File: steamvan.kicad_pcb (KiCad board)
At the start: 2 copper layers, 0 parts

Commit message: Add: new minivan layouts, and start switching to MX/Alps hybrid footprints
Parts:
- added C1: 30p, Capacitor_SMD:C_0603_1608Metric, F.Cu at (-222.7, 200.6)
- added C10: 1u, Capacitor_SMD:C_0603_1608Metric, F.Cu at (-221.6, 197.2)
- added C11: 1u, Capacitor_SMD:C_0603_1608Metric, F.Cu at (-226.3, 203.6)
- added C2: 30p, Capacitor_SMD:C_0603_1608Metric, F.Cu at (-218.5, 195.7)
- added C3: 100n, Capacitor_SMD:C_0603_1608Metric, F.Cu at (-221.6, 194.2)
- added C4: 100n, Capacitor_SMD:C_0603_1608Metric, F.Cu at (-229.3, 202.9)
- added C5: 4.7u, Capacitor_SMD:C_0603_1608Metric, F.Cu at (-225.5, 202.1)
- added C6: 1u, Capacitor_SMD:C_0603_1608Metric, F.Cu at (-229.3, 204.4)
- added C7: 10n, Capacitor_SMD:C_0603_1608Metric, F.Cu at (-218.5, 194.2)
- added C8: 100n, Capacitor_SMD:C_0603_1608Metric, F.Cu at (-221.6, 195.7)
- added C9: 100n, Capacitor_SMD:C_0603_1608Metric, F.Cu at (-222.7, 199.1)
- added D1: D, Diode_SMD:D_SOD-123, F.Cu at (-176.2, 181.4)
- added D10: D, Diode_SMD:D_SOD-123, F.Cu at (-203.8, 181.4)
- added D11: D, Diode_SMD:D_SOD-123, F.Cu at (-207.2, 181.4)
- added D12: D, Diode_SMD:D_SOD-123, F.Cu at (-210.7, 181.4)
- added D13: D, Diode_SMD:D_SOD-123, F.Cu at (-214.1, 181.4)
- added D14: D, Diode_SMD:D_SOD-123, F.Cu at (-217.6, 181.4)
- added D15: D, Diode_SMD:D_SOD-123, F.Cu at (-221.0, 181.4)
- added D16: D, Diode_SMD:D_SOD-123, F.Cu at (-224.5, 181.4)
- added D17: D, Diode_SMD:D_SOD-123, F.Cu at (-227.9, 181.4)
- added D18: D, Diode_SMD:D_SOD-123, F.Cu at (-231.4, 181.4)
- added D19: D, Diode_SMD:D_SOD-123, F.Cu at (-234.8, 181.4)
- added D2: D, Diode_SMD:D_SOD-123, F.Cu at (-179.6, 181.4)
- added D20: D, Diode_SMD:D_SOD-123, F.Cu at (-169.3, 181.4)
- added D21: D, Diode_SMD:D_SOD-123, F.Cu at (-238.3, 181.4)
- added D22: D, Diode_SMD:D_SOD-123, F.Cu at (-245.2, 181.4)
- added D23: D, Diode_SMD:D_SOD-123, F.Cu at (-183.1, 181.4)
- added D24: D, Diode_SMD:D_SOD-123, F.Cu at (-135.1, 221.1)
- added D25: D, Diode_SMD:D_SOD-123, F.Cu at (-96.7, 182.7)
- added D26: D, Diode_SMD:D_SOD-123, F.Cu at (-130.4, 221.1)
- added D27: D, Diode_SMD:D_SOD-123, F.Cu at (-92.0, 182.7)
- added D28: D, Diode_SMD:D_SOD-123, F.Cu at (-96.7, 185.0)
- added D29: D, Diode_SMD:D_SOD-123, F.Cu at (-96.7, 187.4)
- added D3: D, Diode_SMD:D_SOD-123, F.Cu at (-241.7, 181.4)
- added D30: D, Diode_SMD:D_SOD-123, F.Cu at (-96.7, 189.7)
- added D31: D, Diode_SMD:D_SOD-123, F.Cu at (-92.0, 185.0)
- added D32: D, Diode_SMD:D_SOD-123, F.Cu at (-96.7, 192.1)
- added D33: D, Diode_SMD:D_SOD-123, F.Cu at (-87.2, 182.7)
- added D34: D, Diode_SMD:D_SOD-123, F.Cu at (-92.0, 187.4)
- added D35: D, Diode_SMD:D_SOD-123, F.Cu at (-125.6, 221.1)
- added D36: D, Diode_SMD:D_SOD-123, F.Cu at (-92.0, 189.7)
- added D37: D, Diode_SMD:D_SOD-123, F.Cu at (-96.7, 194.4)
- added D38: D, Diode_SMD:D_SOD-123, F.Cu at (-87.2, 185.0)
- added D39: D, Diode_SMD:D_SOD-123, F.Cu at (-92.0, 192.1)
- added D4: D, Diode_SMD:D_SOD-123, F.Cu at (-172.7, 181.4)
- added D40: D, Diode_SMD:D_SOD-123, F.Cu at (-96.7, 196.8)
- added D41: D, Diode_SMD:D_SOD-123, F.Cu at (-82.5, 182.7)
- added D42: D, Diode_SMD:D_SOD-123, F.Cu at (-87.2, 187.4)
- added D43: D, Diode_SMD:D_SOD-123, F.Cu at (-120.9, 221.1)
- added D44: D, Diode_SMD:D_SOD-123, F.Cu at (-87.2, 189.7)
- added D45: D, Diode_SMD:D_SOD-123, F.Cu at (-96.7, 199.1)
- added D46: D, Diode_SMD:D_SOD-123, F.Cu at (-92.0, 194.4)
- added D5: D, Diode_SMD:D_SOD-123, F.Cu at (-186.5, 181.4)
- added D6: D, Diode_SMD:D_SOD-123, F.Cu at (-190.0, 181.4)
- added D7: D, Diode_SMD:D_SOD-123, F.Cu at (-193.4, 181.4)
- added D8: D, Diode_SMD:D_SOD-123, F.Cu at (-196.9, 181.4)
- added D9: D, Diode_SMD:D_SOD-123, F.Cu at (-200.3, 181.4)
- added F1: 500mA, Resistor_SMD:R_0805_2012Metric, F.Cu at (-245.2, 204.3)
- added J1: Conn_01x05_Male, Connector_PinHeader_2.54mm:PinHeader_1x05_P2.54mm_Vertical, F.Cu at (-245.1, 191.3)
- added K_,1: MX-1U, MX_Alps_Hybrid:MX-1U, F.Cu at (247.7, 103.2)
- added K_.1: MX-1U, MX_Alps_Hybrid:MX-1U, F.Cu at (266.7, 103.2)
- added K_/1: MX-1U, MX_Alps_Hybrid:MX-1U, F.Cu at (285.8, 103.2)
- added K_;1: MX-1U, MX_Alps_Hybrid:MX-1U, F.Cu at (276.2, 84.1)
- added K_A1: MX-1U, MX_Alps_Hybrid:MX-1U, F.Cu at (104.8, 84.1)
- added K_B1: MX-1U, MX_Alps_Hybrid:MX-1U, F.Cu at (190.5, 103.2)
- added K_BACK1: MX-1.75U, MX_Alps_Hybrid:MX-1.75U, F.Cu at (297.7, 65.1)
- added K_C1: MX-1U, MX_Alps_Hybrid:MX-1U, F.Cu at (152.4, 103.2)
- added K_D1: MX-1U, MX_Alps_Hybrid:MX-1U, F.Cu at (142.9, 84.1)
- added K_DOWN1: MX-1U, MX_Alps_Hybrid:MXOnly-1U, F.Cu at (285.8, 122.2)
- added K_E1: MX-1U, MX_Alps_Hybrid:MX-1U, F.Cu at (138.1, 65.1)
- added K_ENTER1: MX-2.25U, MX_Alps_Hybrid:MXOnly-2.25U-ReversedStabilizers, F.Cu at (169.1, 122.2)
- added K_F1: MX-1U, MX_Alps_Hybrid:MX-1U, F.Cu at (161.9, 84.1)
- added K_FN1: MX-1.25U, MX_Alps_Hybrid:MX-1.25U, F.Cu at (83.3, 84.1)
- added K_FN2: MX-1.5U, MX_Alps_Hybrid:MX-1.5U, F.Cu at (300.0, 84.1)
- added K_FN3: MX-1U, MX_Alps_Hybrid:MX-1U, F.Cu at (304.8, 103.2)
- added K_FN4: MX-1.5U, MX_Alps_Hybrid:MXOnly-1.5U, F.Cu at (109.5, 122.2)
- added K_FN4_2: MX-1U, MX_Alps_Hybrid:MX-1U, F.Cu at (-108.7, 210.3)
- added K_G1: MX-1U, MX_Alps_Hybrid:MX-1U, F.Cu at (181.0, 84.1)
- added K_H1: MX-1U, MX_Alps_Hybrid:MX-1U, F.Cu at (200.0, 84.1)
- added K_I1: MX-1U, MX_Alps_Hybrid:MX-1U, F.Cu at (233.4, 65.1)
- added K_J1: MX-1U, MX_Alps_Hybrid:MX-1U, F.Cu at (219.1, 84.1)
- added K_K1: MX-1U, MX_Alps_Hybrid:MX-1U, F.Cu at (238.1, 84.1)
- added K_L1: MX-1U, MX_Alps_Hybrid:MX-1U, F.Cu at (257.2, 84.1)
- added K_LALT1: MX-1U, MX_Alps_Hybrid:MX-1U, F.Cu at (-108.7, 191.1)
- added K_LCTL1: MX-1.25U, MX_Alps_Hybrid:MXOnly-1.25U, F.Cu at (83.3, 122.2)
- added K_LCTL2: MX-1U, MX_Alps_Hybrid:MX-1U, F.Cu at (-127.9, 210.3)
- added K_LOCK1: MX-1.75U, MX_Alps_Hybrid:MXOnly-1.75U, F.Cu at (297.7, 122.2)
- added K_LSHIFT1: MX-1.75U, MX_Alps_Hybrid:MX-1.75U, F.Cu at (88.1, 103.2)
- added K_M1: MX-1U, MX_Alps_Hybrid:MX-1U, F.Cu at (228.6, 103.2)
- added K_N1: MX-1U, MX_Alps_Hybrid:MX-1U, F.Cu at (209.6, 103.2)
- added K_O1: MX-1U, MX_Alps_Hybrid:MX-1U, F.Cu at (252.4, 65.1)
- added K_P1: MX-1U, MX_Alps_Hybrid:MX-1U, F.Cu at (271.5, 65.1)
- added K_Q1: MX-1U, MX_Alps_Hybrid:MX-1U, F.Cu at (100.0, 65.1)
- added K_R1: MX-1U, MX_Alps_Hybrid:MX-1U, F.Cu at (157.2, 65.1)
- added K_RALT1: MX-1.25U, MX_Alps_Hybrid:MXOnly-1.25U, F.Cu at (240.5, 122.2)
- added K_RALT2: MX-1.5U, MX_Alps_Hybrid:MXOnly-1.5U-FLIPPED, F.Cu at (242.9, 122.2)
- added K_RIGHT1: MX-1U, MX_Alps_Hybrid:MXOnly-1U, F.Cu at (304.8, 122.2)
- added K_RSHIFT1: MX-1.5U, MX_Alps_Hybrid:MXOnly-1.5U, F.Cu at (266.7, 122.2)
- added K_S1: MX-1U, MX_Alps_Hybrid:MX-1U, F.Cu at (123.8, 84.1)
- added K_SPACE1: MX-2U, MX_Alps_Hybrid:MXOnly-2U-ReversedStabilizers, F.Cu at (209.6, 122.2)
- added K_SUPER1: MX-1.25U, MX_Alps_Hybrid:MXOnly-1.25U, F.Cu at (135.7, 122.2)
- added K_SUPER2: MX-1U, MX_Alps_Hybrid:MX-1U, F.Cu at (-127.9, 191.1)
- added K_T1: MX-1U, MX_Alps_Hybrid:MX-1U, F.Cu at (176.2, 65.1)
- added K_TAB1: MX-1U, MX_Alps_Hybrid:MX-1U, F.Cu at (81.0, 65.1)
- added K_U1: MX-1U, MX_Alps_Hybrid:MX-1U, F.Cu at (214.3, 65.1)
- added K_V1: MX-1U, MX_Alps_Hybrid:MX-1U, F.Cu at (171.4, 103.2)
- added K_W1: MX-1U, MX_Alps_Hybrid:MX-1U, F.Cu at (119.1, 65.1)
- added K_X1: MX-1U, MX_Alps_Hybrid:MX-1U, F.Cu at (133.3, 103.2)
- added K_Y1: MX-1U, MX_Alps_Hybrid:MX-1U, F.Cu at (195.3, 65.1)
- added K_Z1: MX-1U, MX_Alps_Hybrid:MX-1U, F.Cu at (114.3, 103.2)
- added Q1: FMMT493TA, digikey-footprints:SOT-23-3, F.Cu at (-221.2, 191.5)
- added R1: 560, Resistor_SMD:R_0603_1608Metric, F.Cu at (-221.3, 183.9)
- added R10: 560, Resistor_SMD:R_0603_1608Metric, F.Cu at (-233.4, 183.9)
- added R11: 560, Resistor_SMD:R_0603_1608Metric, F.Cu at (-245.4, 185.4)
- added R12: 560, Resistor_SMD:R_0603_1608Metric, F.Cu at (-242.4, 185.4)
- added R13: 560, Resistor_SMD:R_0603_1608Metric, F.Cu at (-239.4, 185.4)
- added R14: 560, Resistor_SMD:R_0603_1608Metric, F.Cu at (-236.4, 185.4)
- added R15: 560, Resistor_SMD:R_0603_1608Metric, F.Cu at (-233.4, 185.4)
- added R16: 560, Resistor_SMD:R_0603_1608Metric, F.Cu at (-230.3, 183.9)
- added R17: 560, Resistor_SMD:R_0603_1608Metric, F.Cu at (-227.3, 183.9)
- added R18: 560, Resistor_SMD:R_0603_1608Metric, F.Cu at (-218.3, 183.9)
- added R19: 560, Resistor_SMD:R_0603_1608Metric, F.Cu at (-203.3, 185.4)
- added R2: 560, Resistor_SMD:R_0603_1608Metric, F.Cu at (-224.3, 185.4)
- added R20: 560, Resistor_SMD:R_0603_1608Metric, F.Cu at (-200.2, 183.9)
- added R21: 560, Resistor_SMD:R_0603_1608Metric, F.Cu at (-203.3, 183.9)
- added R22: 560, Resistor_SMD:R_0603_1608Metric, F.Cu at (-206.3, 185.4)
- added R23: 560, Resistor_SMD:R_0603_1608Metric, F.Cu at (-206.3, 183.9)
- added R24: 560, Resistor_SMD:R_0603_1608Metric, F.Cu at (-209.3, 185.4)
- added R25: 560, Resistor_SMD:R_0603_1608Metric, F.Cu at (-212.3, 185.4)
- added R26: 560, Resistor_SMD:R_0603_1608Metric, F.Cu at (-215.3, 185.4)
- added R27: 560, Resistor_SMD:R_0603_1608Metric, F.Cu at (-209.3, 183.9)
- added R28: 560, Resistor_SMD:R_0603_1608Metric, F.Cu at (-212.3, 183.9)
- added R29: 560, Resistor_SMD:R_0603_1608Metric, F.Cu at (-215.3, 183.9)
- added R3: 560, Resistor_SMD:R_0603_1608Metric, F.Cu at (-227.3, 185.4)
- added R30: 560, Resistor_SMD:R_0603_1608Metric, F.Cu at (-218.3, 185.4)
- added R31: 560, Resistor_SMD:R_0603_1608Metric, F.Cu at (-245.4, 183.9)
- added R32: 560, Resistor_SMD:R_0603_1608Metric, F.Cu at (-197.2, 183.9)
- added R33: 560, Resistor_SMD:R_0603_1608Metric, F.Cu at (-200.2, 185.4)
- added R34: 560, Resistor_SMD:R_0603_1608Metric, F.Cu at (-221.3, 185.4)
- added R35: 560, Resistor_SMD:R_0603_1608Metric, F.Cu at (-194.2, 183.9)
- added R36: 560, Resistor_SMD:R_0603_1608Metric, F.Cu at (-197.2, 185.4)
- added R37: 560, Resistor_SMD:R_0603_1608Metric, F.Cu at (-194.2, 185.4)
- added R38: 560, Resistor_SMD:R_0603_1608Metric, F.Cu at (-191.2, 185.4)
- added R39: 560, Resistor_SMD:R_0603_1608Metric, F.Cu at (-188.2, 183.9)
- added R4: 560, Resistor_SMD:R_0603_1608Metric, F.Cu at (-230.3, 185.4)
- added R40: 560, Resistor_SMD:R_0603_1608Metric, F.Cu at (-185.2, 183.9)
- added R41: 560, Resistor_SMD:R_0603_1608Metric, F.Cu at (-188.2, 185.4)
- added R42: 560, Resistor_SMD:R_0603_1608Metric, F.Cu at (-185.2, 185.4)
- added R43: 560, Resistor_SMD:R_0603_1608Metric, F.Cu at (-182.2, 183.9)
- added R44: 560, Resistor_SMD:R_0603_1608Metric, F.Cu at (-179.2, 183.9)
- added R45: 560, Resistor_SMD:R_0603_1608Metric, F.Cu at (-182.2, 185.4)
- added R46: 560, Resistor_SMD:R_0603_1608Metric, F.Cu at (-83.3, 184.6)
- added R5: 560, Resistor_SMD:R_0603_1608Metric, F.Cu at (-224.3, 183.9)
- added R6: 560, Resistor_SMD:R_0603_1608Metric, F.Cu at (-191.2, 183.9)
- added R7: 560, Resistor_SMD:R_0603_1608Metric, F.Cu at (-242.4, 183.9)
- added R8: 560, Resistor_SMD:R_0603_1608Metric, F.Cu at (-239.4, 183.9)
- added R9: 560, Resistor_SMD:R_0603_1608Metric, F.Cu at (-236.4, 183.9)
- added RC1: 470, Resistor_SMD:R_0603_1608Metric, F.Cu at (-222.5, 202.1)
- added RC6: 5.1k, Resistor_SMD:R_0603_1608Metric, F.Cu at (-218.5, 197.2)
- added RC7: 5.1k, Resistor_SMD:R_0603_1608Metric, F.Cu at (-226.3, 205.1)
- added RC8: 10k, Resistor_SMD:R_0603_1608Metric, F.Cu at (-219.7, 198.7)
- added SW1: SW_Push, Button_Switch_SMD:SW_SPST_TL3342, F.Cu at (-239.0, 203.1)
- added U1: STM32F303CBTx, Package_QFP:LQFP-48_7x7mm_P0.5mm, F.Cu at (-238.0, 194.8)
- added U2: TLV70233_SOT23-5, Package_TO_SOT_SMD:SOT-23-5, F.Cu at (-232.8, 204.0)
- added U3: NUF2221W1T2G, digikey-footprints:SOT-363, F.Cu at (-225.6, 199.8)
- added USB1: HRO-TYPE-C-31-M-12, Type-C:HRO-TYPE-C-31-M-12-Assembly, F.Cu at (-227.9, 198.1)
- added Y1: 8MHz, Crystal:Crystal_SMD_5032-4Pin_5.0x3.2mm, F.Cu at (-229.9, 200.2)

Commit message: Update: Work on PCB component placement
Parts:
- C1, C10, C11, C2, C3, C4, C5, C6, C7, C8, C9, D1, D10, D11, D12, D13, D14, D15, D16, D17, D18, D19, D2, D20, D21, D22, D23, D24, D25, D26, D27, D28, D29, D3, D30, D31, D32, D33, D34, D35, D36, D37, D38, D39, D4, D40, D41, D42, D43, D44, D45, D46, D5, D6, D7, D8, D9, F1, J1, Q1, R1, R10, R11, R12, R13, R14, R15, R16, R17, R18, R19, R2, R20, R21, R22, R23, R24, R25, R26, R27, R28, R29, R3, R30, R31, R32, R33, R34, R35, R36, R37, R38, R39, R4, R40, R41, R42, R43, R44, R45, R46, R5, R6, R7, R8, R9, RC1, RC6, RC7, RC8, SW1, U1, U2, U3, USB1, Y1: moved to B.Cu
- K_,1, K_.1, K_/1, K_;1, K_A1, K_B1, K_C1, K_D1, K_E1, K_F1, K_FN3, K_FN4_2, K_G1, K_H1, K_I1, K_J1, K_K1, K_L1, K_LALT1, K_M1, K_N1, K_O1, K_P1, K_Q1, K_R1, K_S1, K_T1, K_TAB1, K_U1, K_V1, K_W1, K_X1, K_Y1, K_Z1: footprint MX_Alps_Hybrid:MX-1U -> MX_Alps_Hybrid:MXOnly-1U
- K_BACK1, K_LSHIFT1: footprint MX_Alps_Hybrid:MX-1.75U -> MX_Alps_Hybrid:MXOnly-1.75U
- K_FN1: footprint MX_Alps_Hybrid:MX-1.25U -> MX_Alps_Hybrid:MXOnly-1.25U
- K_FN2: footprint MX_Alps_Hybrid:MX-1.5U -> MX_Alps_Hybrid:MXOnly-1.5U
- K_LCTL2, K_SUPER2: footprint MX_Alps_Hybrid:MX-1U -> MX_Alps_Hybrid:MXOnly-1U-FLIPPED
- moved R12 560.0 mm to (305.6, 69.8), turned to 90 degrees
- moved R11 537.4 mm to (279.4, 69.8), turned to 90 degrees
- moved D12 530.2 mm to (306.4, 64.3), turned to 90 degrees
- moved R24 526.2 mm to (308.0, 88.9), turned to 90 degrees
- moved D22 520.4 mm to (265.9, 83.3), turned to 90 degrees
- moved R36 515.8 mm to (312.7, 108.0), turned to 90 degrees
- moved R10 506.7 mm to (260.4, 69.8), turned to 90 degrees
- moved R34 502.0 mm to (274.6, 108.0), turned to 90 degrees
- moved D11 501.3 mm to (280.2, 64.3), turned to 90 degrees
- moved R23 499.5 mm to (284.2, 88.9), turned to 90 degrees
- moved D21 494.9 mm to (246.9, 83.3), turned to 90 degrees
- moved R35 493.8 mm to (293.7, 108.0), turned to 90 degrees
- moved R9 491.1 mm to (241.3, 69.8), turned to 90 degrees
- moved R22 481.2 mm to (265.1, 88.9), turned to 90 degrees
- moved D10 479.4 mm to (261.1, 64.3), turned to 90 degrees
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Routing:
- net Net-(K_Q1-Pad4): track 0.00 -> 0.80 mm
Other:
- net class Default: clearance 0.2 -> 0.2032; trace_width 0.25 -> 0.254
- net class Power added: clearance 0.2032, trace_width 0.381, via_dia 0.8, via_drill 0.4
- rule trace_clearance: 0.2 -> 0.2032

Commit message: Update: Work on PCB layout
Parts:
- moved J1 167.0 mm to (310.9, 76.1)
- moved USB1 147.3 mm to (286.0, 54.0)
- moved RC7 142.2 mm to (293.0, 58.3), turned to 270 degrees
- moved F1 141.7 mm to (279.1, 64.9), turned to 90 degrees
- moved U2 135.2 mm to (291.5, 74.7), turned to 180 degrees
- moved C10 135.1 mm to (295.9, 74.3), turned to 270 degrees
- moved RC6 134.9 mm to (279.5, 58.5), turned to 270 degrees
- moved U3 134.1 mm to (285.8, 67.3), turned to 180 degrees
- moved C11 133.0 mm to (291.4, 71.1)
- moved Q1 126.3 mm to (276.9, 74.9), turned to 90 degrees
- moved SW1 118.9 mm to (77.8, 109.5), turned to 90 degrees
- moved RC1 115.0 mm to (275.8, 79.1), turned to 270 degrees
- moved C8 56.8 mm to (183.1, 117.7), turned to 270 degrees
- moved C5 54.4 mm to (193.7, 111.0), turned to 180 degrees
- moved U1 53.9 mm to (189.7, 119.1), turned to 90 degrees
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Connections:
- K_ENTER1 pad 1: COL5 -> COL4
- K_SPACE1 pad 1: COL7 -> COL6
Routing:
- net LEDGND: track 0.00 -> 833.6 mm
- net +5V: track 0.00 -> 826.9 mm
- net ROW1: track 0.00 -> 232.5 mm
- net ROW2: track 0.00 -> 231.7 mm
- net ROW3: track 0.00 -> 199.7 mm
- net ROW0: track 0.00 -> 188.0 mm
- net COL3: track 0.00 -> 72.4 mm
- net COL11: track 0.00 -> 70.5 mm
- net COL2: track 0.00 -> 69.0 mm
- net COL8: track 0.00 -> 67.4 mm
- net COL1: track 0.00 -> 65.0 mm
- net COL0: track 0.00 -> 64.5 mm
- net COL4: track 0.00 -> 64.1 mm
- net COL6: track 0.00 -> 63.1 mm
- net COL10: track 0.00 -> 63.1 mm
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
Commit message: Add: PCB footprint
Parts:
- added REF**: minivan_outline, jmdaly_keyboard_parts:minivan_outline, F.Cu at (102.8, 74.6)
- moved D43 20.1 mm to (231.5, 121.4)
- moved R11 3.18 mm to (276.6, 68.3)
- moved R19 2.48 mm to (205.5, 88.9)
- moved Q1 2.42 mm to (274.4, 75.1)
- moved USB1 0.53 mm to (285.6, 53.6)
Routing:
- net +5V: track 826.9 -> 785.2 mm
- net Net-(D43-Pad2): track 9.66 -> 15.4 mm
- net LEDGND: track 833.6 -> 830.3 mm
- net Net-(K_P1-Pad4): track 6.86 -> 4.31 mm
- net Net-(K_H1-Pad4): track 6.86 -> 4.40 mm
- net ROW3: track 199.7 -> 198.4 mm
- net (no net): track 0.00 -> 0.85 mm
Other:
- board outline added: 243.4 x 76.7 mm

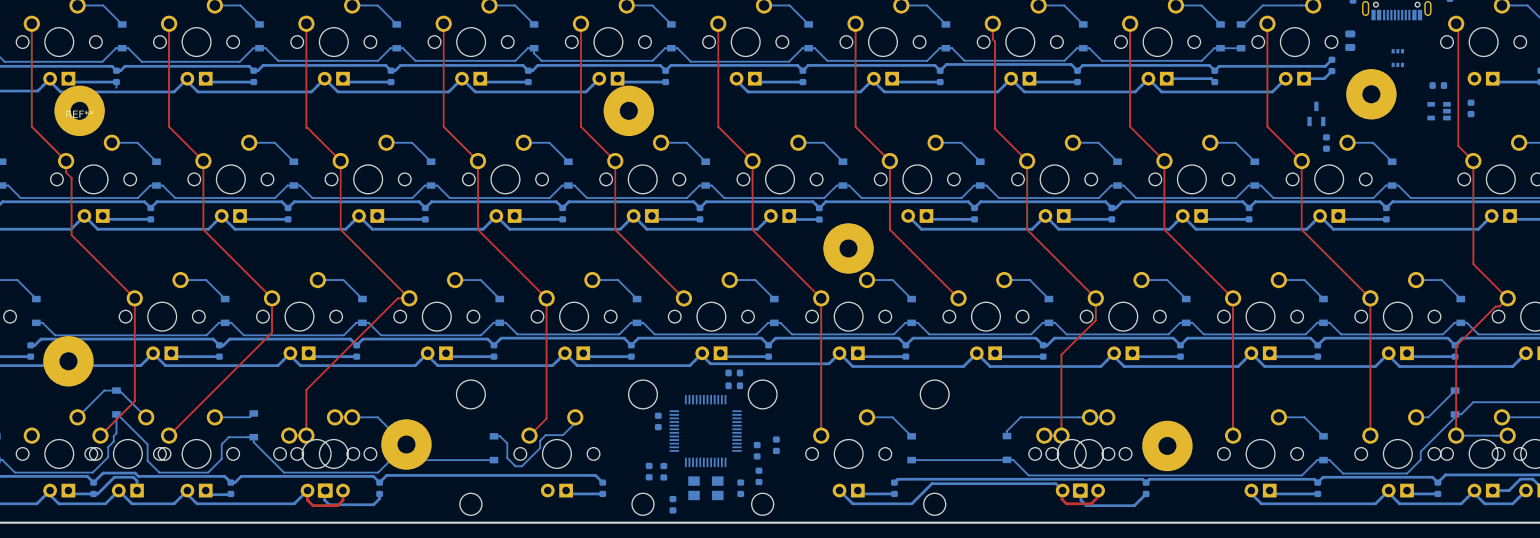
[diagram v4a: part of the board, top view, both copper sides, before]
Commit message: Update: PCB footprint, and work on component placement
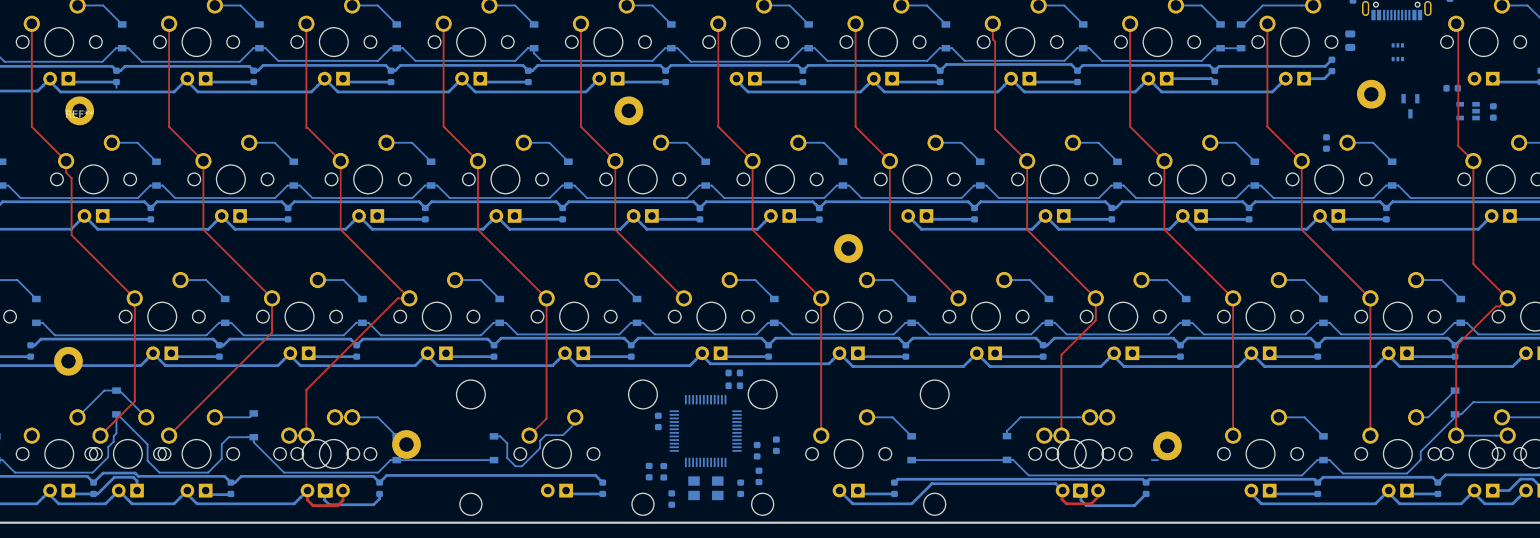
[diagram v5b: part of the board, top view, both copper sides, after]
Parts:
- moved Q1 13.1 mm to (287.5, 74.0), turned to 270 degrees
- moved U2 4.04 mm to (295.5, 74.7)
- moved C10 3.13 mm to (299.0, 74.8)
- moved C11 1.96 mm to (293.3, 71.5)
- moved U3 0.81 mm to (285.8, 66.5)
- moved C1 0.80 mm to (185.0, 128.5)
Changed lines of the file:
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@@
     (fp_arc (start -28.65 54.149901) (end -31.65 54.149901) (angle -90) (layer Edge.Cuts) (width 0.3))
     (fp_arc (start 208.737293 54.149901) (end 208.737293 57.149901) (angle -90) (layer Edge.Cuts) (width 0.3))
-    (pad 1 thru_hole circle (at 150.9373 46.4999) (size 7.0013 7.0013) (drill 2.4994) (layers *.Cu *.Mask))
-    (pad 1 thru_hole circle (at 179.2373 -2.3) (size 7.0013 7.0013) (drill 2.4994) (layers *.Cu *.Mask))
-    (pad 1 thru_hole circle (at 106.6873 19.1) (size 7.0013 7.0013) (drill 2.4994) (layers *.Cu *.Mask))
-    (pad 1 thru_hole circle (at 76.2 0) (size 7.0013 7.0013) (drill 2.4994) (layers *.Cu *.Mask))
-    (pad 1 thru_hole circle (at 45.35 46.2999) (size 7.0013 7.0013) (drill 2.4994) (layers *.Cu *.Mask))
-    (pad 1 thru_hole circle (at -1.55 34.7499) (size 7.0013 7.0013) (drill 2.4994) (layers *.Cu *.Mask))
-    (pad 1 thru_hole circle (at 0 0) (size 7.0013 7.0013) (drill 2.4994) (layers *.Cu *.Mask))
+    (pad 1 thru_hole circle (at 150.9373 46.4999) (size 4 4) (drill 2) (layers *.Cu *.Mask))
+    (pad 1 thru_hole circle (at 179.2373 -2.3) (size 4 4) (drill 2) (layers *.Cu *.Mask))
+    (pad 1 thru_hole circle (at 106.6873 19.1) (size 4 4) (drill 2) (layers *.Cu *.Mask))
+    (pad 1 thru_hole circle (at 76.2 0) (size 4 4) (drill 2) (layers *.Cu *.Mask))
+    (pad 1 thru_hole circle (at 45.35 46.2999) (size 4 4) (drill 2) (layers *.Cu *.Mask))
+    (pad 1 thru_hole circle (at -1.55 34.7499) (size 4 4) (drill 2) (layers *.Cu *.Mask))
+    (pad 1 thru_hole circle (at 0 0) (size 4 4) (drill 2) (layers *.Cu *.Mask))
   )
   (module Capacitor_SMD:C_0603_1608Metric (layer B.Cu)
-    (at 185.166 129.286 270)
+    (at 185 128.5 270)
     (descr "Capacitor SMD 0603 (1608 Metric), square (rectangular) end terminal, IPC_7351 nominal, (Body size source: http://www.tortai-tech.com/upload/download/2011102023233369053.pdf), generated with kicad-footprint-generator")
     (tags capacitor)
@@
   )
   (module Capacitor_SMD:C_0603_1608Metric (layer B.Cu)
-    (at 295.91 74.295 270)
+    (at 299 74.7875 270)
     (descr "Capacitor SMD 0603 (1608 Metric), square (rectangular) end terminal, IPC_7351 nominal, (Body size source: http://www.tortai-tech.com/upload/download/2011102023233369053.pdf), generated with kicad-footprint-generator")
     (tags capacitor)
@@
   )
   (module Capacitor_SMD:C_0603_1608Metric (layer B.Cu)
-    (at 291.3635 71.12)
+    (at 293.2875 71.5)
     (descr "Capacitor SMD 0603 (1608 Metric), square (rectangular) end terminal, IPC_7351 nominal, (Body size source: http://www.tortai-tech.com/upload/download/2011102023233369053.pdf), generated with kicad-footprint-generator")
     (tags capacitor)
@@
   )
   (module digikey-footprints:SOT-23-3 (layer B.Cu)
-    (at 274.447 75.057 90)
-    (fp_text reference Q1 (at 0.025 3.375 90) (layer B.SilkS)
-      (effects (font (size 1 1) (thickness 0.15)) (justify mirror))
-    )
-    (fp_text value FMMT493TA (at 0.025 -3.25 90) (layer B.Fab)
+    (at 287.5 74 270)
+    (fp_text reference Q1 (at 0.025 3.375 270) (layer B.SilkS)
+      (effects (font (size 1 1) (thickness 0.15)) (justify mirror))
+    )
+    (fp_text value FMMT493TA (at 0.025 -3.25 270) (layer B.Fab)
       (effects (font (size 1 1) (thickness 0.15)) (justify mirror))
     )
@@
     (fp_line (start 0.45 1.65) (end 0.825 1.65) (layer B.SilkS) (width 0.1))
     (fp_line (start 0.825 1.65) (end 0.825 1.35) (layer B.SilkS) (width 0.1))
-    (fp_text user %R (at -0.125 -0.15 90) (layer B.Fab)
+    (fp_text user %R (at -0.125 -0.15 270) (layer B.Fab)
       (effects (font (size 0.25 0.25) (thickness 0.05)) (justify mirror))
     )
     (fp_line (start -0.7 -1.52) (end 0.7 -1.52) (layer B.Fab) (width 0.1))
     (fp_line (start 0.7 -1.52) (end 0.7 1.52) (layer B.Fab) (width 0.1))
-    (pad 3 smd rect (at 1.05 0 90) (size 1.3 0.6) (layers B.Cu B.Paste B.Mask)
+    (pad 3 smd rect (at 1.05 0 270) (size 1.3 0.6) (layers B.Cu B.Paste B.Mask)
       (net 93 LEDGND) (solder_mask_margin 0.07))
-    (pad 2 smd rect (at -1.05 -0.95 90) (size 1.3 0.6) (layers B.Cu B.Paste B.Mask)
+    (pad 2 smd rect (at -1.05 -0.95 270) (size 1.3 0.6) (layers B.Cu B.Paste B.Mask)
       (net 2 GND) (solder_mask_margin 0.07))
-    (pad 1 smd rect (at -1.05 0.95 90) (size 1.3 0.6) (layers B.Cu B.Paste B.Mask)
+    (pad 1 smd rect (at -1.05 0.95 270) (size 1.3 0.6) (layers B.Cu B.Paste B.Mask)
       (net 94 "Net-(Q1-Pad1)") (solder_mask_margin 0.07))
   )
@@
   )
   (module Package_TO_SOT_SMD:SOT-23-5 (layer B.Cu)
-    (at 291.465 74.676 180)
+    (at 295.5 74.676 180)
     (descr "5-pin SOT23 package")
     (tags SOT-23-5)
@@
   )
   (module digikey-footprints:SOT-363 (layer B.Cu)
-    (at 285.75 67.31 180)
+    (at 285.75 66.5 180)
     (fp_text reference U3 (at 0 2.159 180) (layer B.SilkS)
       (effects (font (size 1 1) (thickness 0.15)) (justify mirror))

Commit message: Update: Work on routing
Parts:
- moved Q1 10.9 mm to (276.6, 73.7), turned to 90 degrees
- moved RC6 1.03 mm to (278.5, 58.5)
- moved C8 0.32 mm to (183.1, 117.4)
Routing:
- net +5V: track 785.2 -> 1423.7 mm
- net D_N: track 0.00 -> 134.9 mm, vias 0 -> 4
- net D_P: track 0.00 -> 134.8 mm, vias 0 -> 4
- net GND: track 0.00 -> 61.4 mm
- net +3V3: track 0.00 -> 31.4 mm
- net OSC_IN: track 0.00 -> 11.2 mm
- net D_NI: track 0.00 -> 8.16 mm
- net OSC_OUT: track 0.00 -> 7.27 mm
- net D_PI: track 0.00 -> 6.74 mm
- net Net-(F1-Pad2): track 0.00 -> 5.74 mm
- net Net-(RC8-Pad1): track 0.00 -> 5.64 mm

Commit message: Update: Work on routing
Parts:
- moved D29 16.9 mm to (163.3, 102.4)
- moved R29 3.11 mm to (176.3, 108.0)
- moved D10 0.79 mm to (260.4, 64.3)
- moved D28 0.73 mm to (160.4, 102.4)
- moved D11 0.35 mm to (263.7, 64.3)
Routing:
- net +3V3: track 31.4 -> 173.0 mm, vias 0 -> 4
- net +5V: track 1423.7 -> 1297.9 mm, vias 0 -> 2
- net LEDPWM: track 0.00 -> 113.9 mm, vias 0 -> 4
- net COL0: track 64.5 -> 159.7 mm, vias 0 -> 1
- net COL1: track 65.0 -> 137.2 mm, vias 0 -> 1
- net COL2: track 69.0 -> 121.3 mm, vias 0 -> 1
- net ROW2: track 231.7 -> 193.1 mm
- net COL3: track 72.5 -> 104.7 mm, vias 0 -> 1
- net COL4: track 64.1 -> 76.4 mm, vias 0 -> 1
- net GND: track 61.4 -> 72.0 mm, vias 0 -> 1
- net Net-(F1-Pad2): track 5.74 -> 14.4 mm, vias 0 -> 2
- net Net-(RC8-Pad1): track 5.64 -> 12.6 mm
- net Net-(D29-Pad2): track 7.28 -> 11.7 mm
- net Net-(Q1-Pad1): track 0.00 -> 4.26 mm
- net LEDGND: track 830.4 -> 833.8 mm, vias 0 -> 2
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
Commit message: Update: Work on routing
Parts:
- moved C3 0.25 mm to (196.8, 122.0)
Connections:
- U1 pad 12: COL0 -> Net-(U1-Pad12)
- U1 pad 16: COL2 -> COL5
- U1 pad 27: COL3 -> COL4
- U1 pad 28: COL4 -> COL3
- U1 pad 29: COL5 -> COL2
- U1 pad 3: COL10 -> Net-(U1-Pad3)
- U1 pad 30: COL6 -> COL1
- U1 pad 31: Net-(U1-Pad31) -> COL0
- U1 pad 38: ROW3 -> COL11
- U1 pad 39: COL8 -> COL10
- U1 pad 4: COL11 -> ROW3
- U1 pad 41: Net-(U1-Pad41) -> COL8
- U1 pad 42: Net-(U1-Pad42) -> COL7
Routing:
- net COL11: track 70.5 -> 187.8 mm, vias 0 -> 3
- net COL10: track 63.1 -> 159.0 mm, vias 0 -> 3
- net COL9: track 63.1 -> 139.9 mm, vias 0 -> 3
- net COL8: track 67.4 -> 125.9 mm, vias 0 -> 3
- net COL7: track 44.0 -> 85.2 mm, vias 0 -> 1
- net COL0: track 159.7 -> 190.8 mm
- net COL1: track 137.2 -> 168.2 mm
- net COL2: track 121.3 -> 152.1 mm
- net COL3: track 104.7 -> 135.4 mm
- net COL4: track 76.4 -> 106.7 mm
